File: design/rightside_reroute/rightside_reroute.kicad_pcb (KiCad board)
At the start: 4 copper layers, 144 x 96.2 mm, 197 parts, among them IC1 BQ27441DRZT-G1A, IC2 XC9148G50CER-G, IC3 nRF52833-QDAA-R7, IC4 74AHCT125PW,118, IC5 MCP23018T-E_SS, IC6 XC9291B33D1R-G, J1 USB_C_Receptacle_USB2.0_16P, J2 Battery Pos, J3 Battery Neg, J4 OLED_128x32, J6 Conn_01x04, J7 F32Q-1A7H1-11012, U2 BQ24072RGT, U3 USB6B1, U5 PEC11L-4015F-S0015, U6 PEC11L-4015F-S0015, Y1 ECS-320-8-37B2-JTY-TR

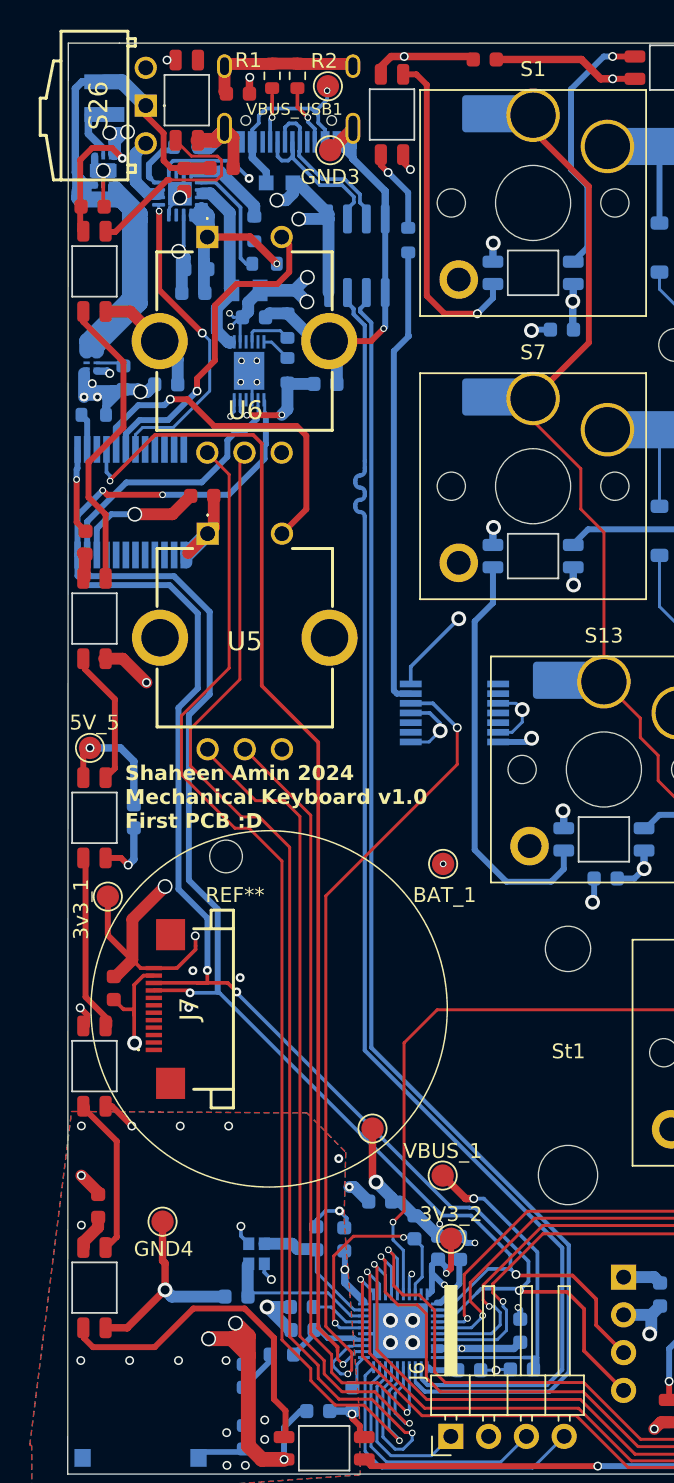
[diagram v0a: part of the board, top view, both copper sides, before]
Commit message: begin to reroute leds
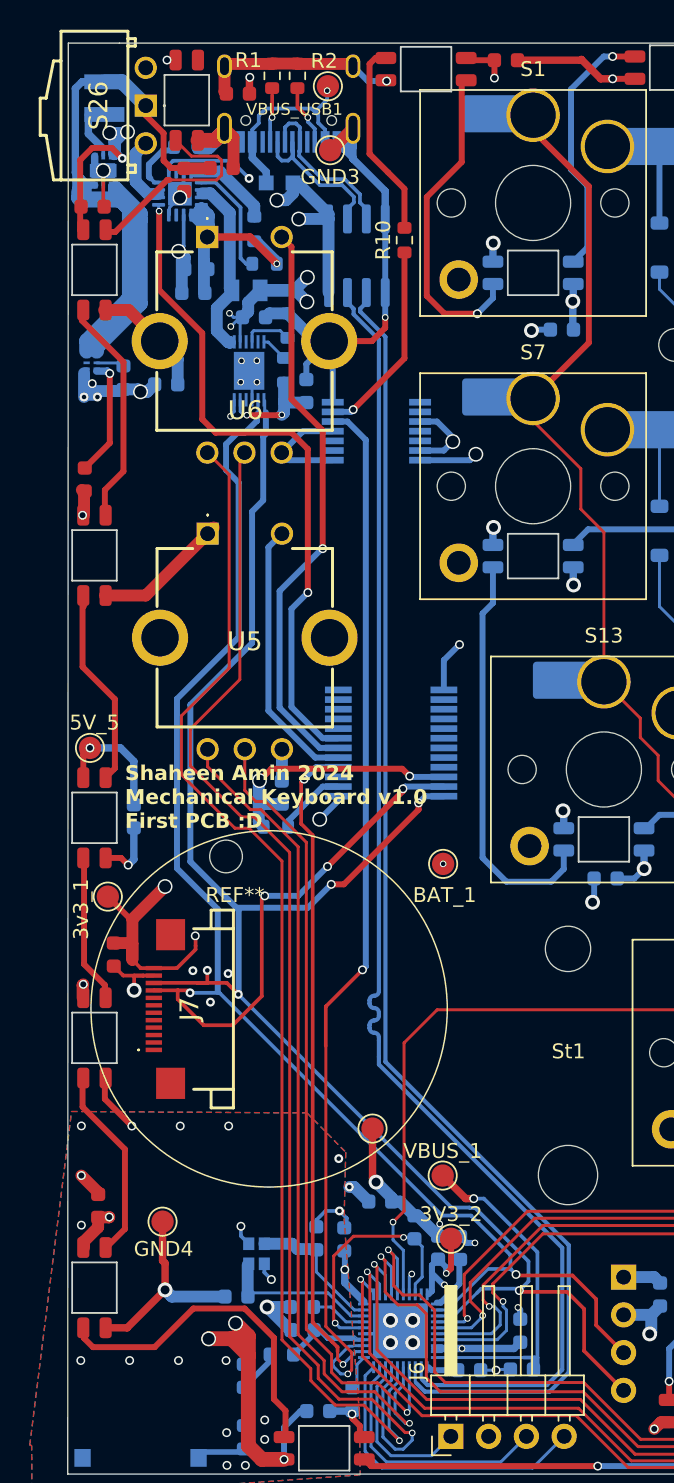
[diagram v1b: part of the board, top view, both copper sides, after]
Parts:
- C20: moved to B.Cu
- R10: moved to F.Cu
- moved R9 30.3 mm to (105.6, 89.3), turned to 180 degrees
- moved IC5 23.9 mm to (113.3, 83.7), turned to 180 degrees
- moved C20 20.7 mm to (106.0, 87.0), turned to -90 degrees
- moved IC4 19.7 mm to (112.3, 62.7)
- moved C46 4.25 mm to (92.7, 66.0)
- moved D46 4.25 mm to (93.4, 71.1)
- moved D1 3.81 mm to (115.7, 38.4), turned to 0 degrees
- moved C37 2.25 mm to (94.7, 97.9)
- moved D44 1.90 mm to (93.4, 103.5)
- moved C42 1.43 mm to (121.0, 37.8)
- moved C22 1.37 mm to (107.6, 60.0), turned to 90 degrees
- moved R10 0.25 mm to (114.2, 49.9)
- moved R8 0.23 mm to (106.1, 58.6)
- moved D47 0.10 mm to (93.4, 51.9)
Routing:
- net /INTA: track 80.1 -> 45.0 mm
- net /CHG: track 21.1 -> 45.4 mm
- net /SCL: track 104.9 -> 123.5 mm, vias 2 -> 5
- net Net-(IC4-2Y): track 31.1 -> 13.4 mm, vias 0 -> 1
- net /NO2: track 21.8 -> 39.1 mm
- net /2A: track 55.6 -> 71.4 mm
- net GND: track 291.1 -> 300.8 mm, vias 105 -> 103
- net Net-(D1-DIN): track 5.70 -> 13.3 mm, vias 1 -> 0
- net 3V3: track 76.5 -> 82.1 mm, vias 13 -> 14
- net Net-(D46-DOUT): track 20.5 -> 15.5 mm
- net Net-(D45-DOUT): track 9.10 -> 14.1 mm
- net /NO: track 22.8 -> 18.3 mm, vias 1 -> 0
- net /SDA: track 112.3 -> 115.2 mm
- net Net-(D43-DOUT): track 10.6 -> 13.1 mm
- net Net-(IC5-~{RESET}): track 2.48 -> 4.71 mm
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
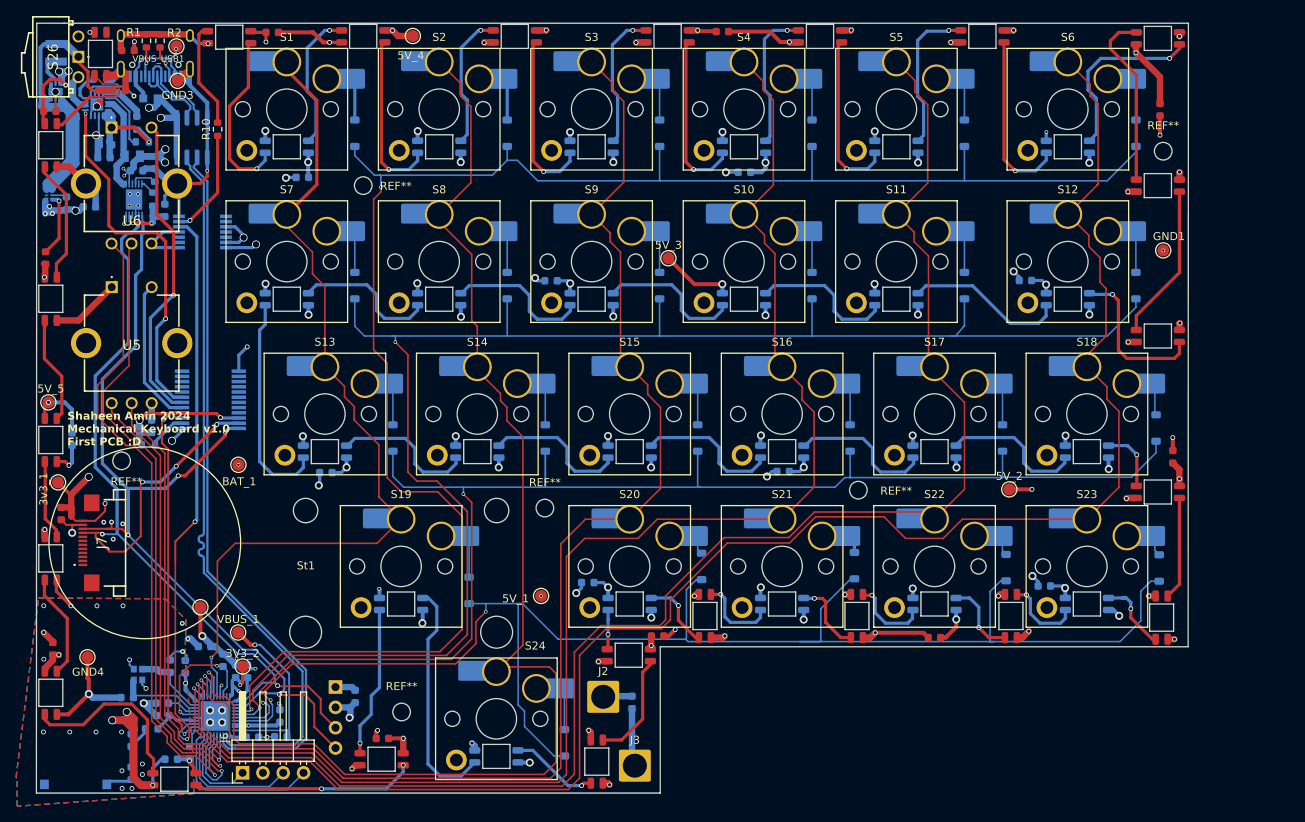
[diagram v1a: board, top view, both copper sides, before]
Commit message: prepare to add cut out for battery
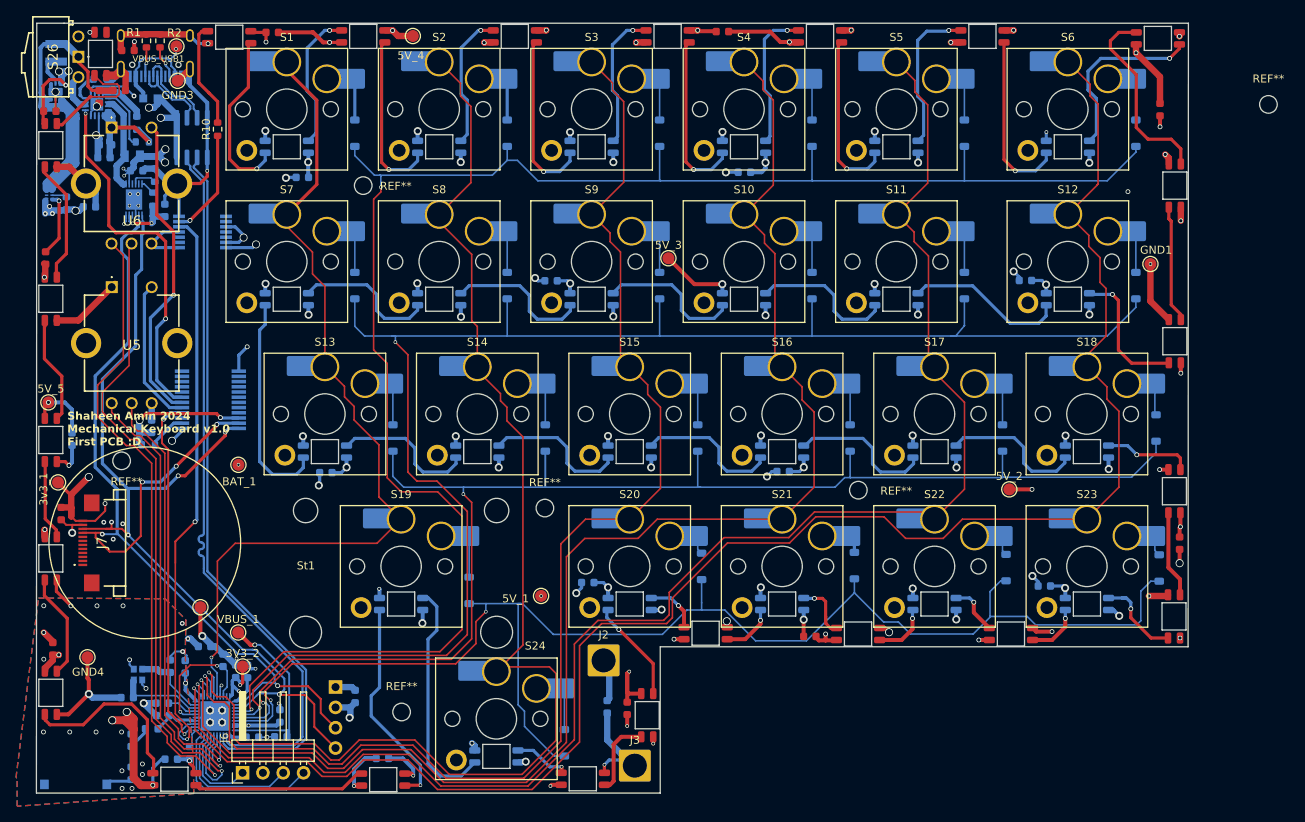
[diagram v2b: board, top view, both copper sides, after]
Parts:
- C45: moved to B.Cu
- moved C43 15.6 mm to (188.2, 113.3), turned to 180 degrees
- moved REF** 14.4 mm to (245.6, 46.8)
- moved C36 10.8 mm to (234.5, 101.6), turned to -90 degrees
- moved C44 9.82 mm to (165.4, 122.3), turned to 90 degrees
- moved D37 7.84 mm to (167.9, 123.1), turned to -90 degrees
- moved J2 4.55 mm to (162.5, 116.3)
- moved C17 3.15 mm to (162.9, 122.1)
- moved D38 2.77 mm to (159.9, 131.1), turned to 180 degrees
- moved D41 2.56 mm to (134.9, 131.2), turned to 180 degrees
- moved C45 2.50 mm to (134.8, 128.5), turned to 0 degrees
- moved GND1 2.33 mm to (230.8, 66.7)
- moved D33 2.25 mm to (194.3, 113.0), turned to 180 degrees
- moved D31 2.25 mm to (213.4, 113.0), turned to 180 degrees
- moved D15 2.22 mm to (233.9, 76.4), turned to -90 degrees
- moved D35 2.15 mm to (175.2, 112.9), turned to 180 degrees
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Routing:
- net GND: track 300.8 -> 324.8 mm, vias 103 -> 101
- net /Row 3: track 189.3 -> 177.6 mm
- net Net-(D36-DOUT): track 4.95 -> 12.9 mm
- net Net-(D40-DOUT): track 18.9 -> 26.8 mm
- net Net-(D41-DOUT): track 27.9 -> 21.7 mm, vias 2 -> 0
- net Net-(D14-DOUT): track 19.5 -> 14.7 mm
- net Net-(D38-DOUT): track 11.1 -> 7.08 mm
- net Net-(D37-DOUT): track 13.7 -> 9.78 mm
- net Net-(D34-DOUT): track 10.3 -> 6.79 mm
- net Net-(D31-DOUT): track 9.64 -> 6.46 mm
- net Net-(D27-DOUT): track 7.94 -> 11.1 mm
- net Net-(D30-DOUT): track 9.92 -> 6.88 mm
- net Net-(D32-DOUT): track 10.0 -> 7.06 mm
- net Net-(D15-DOUT): track 19.9 -> 17.2 mm
- net Net-(D35-DOUT): track 9.08 -> 6.77 mm
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
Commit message: prepare to correct bq27441
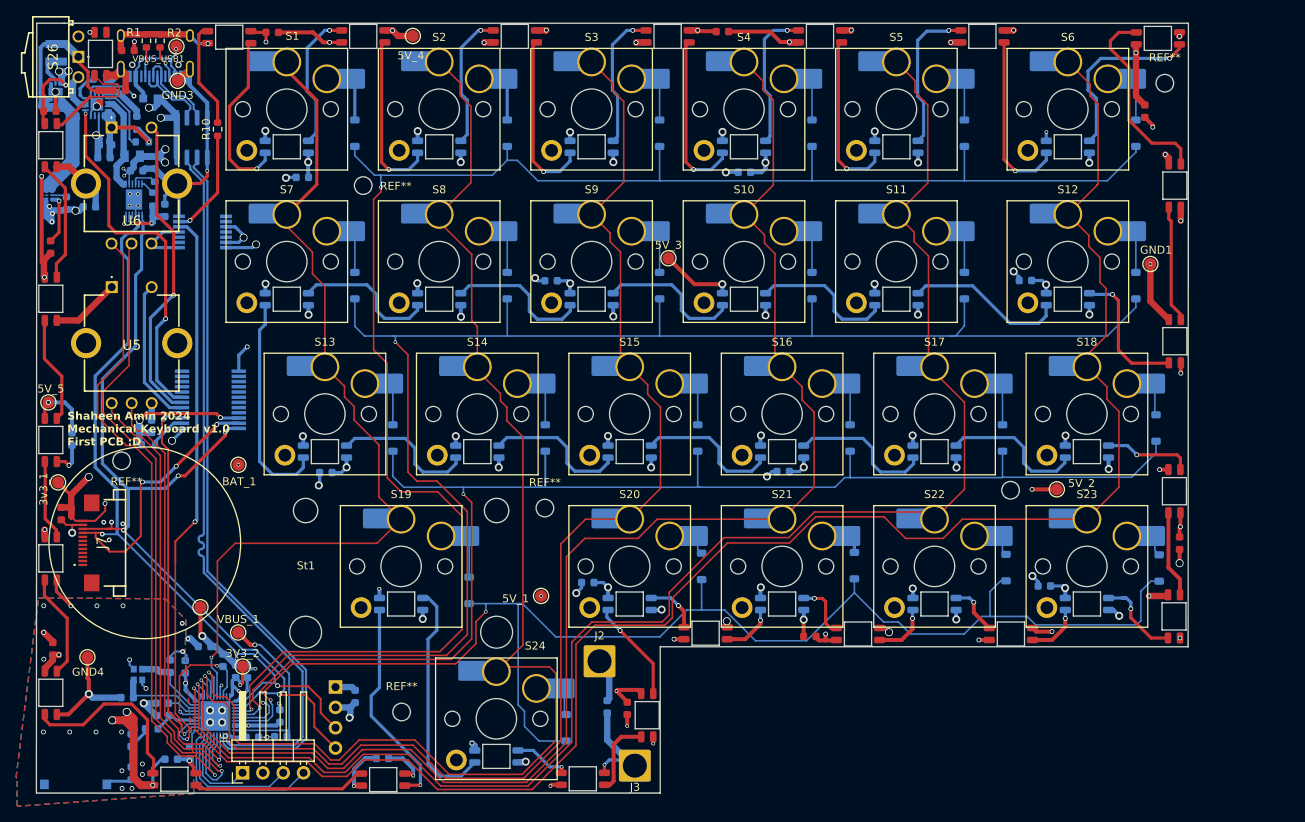
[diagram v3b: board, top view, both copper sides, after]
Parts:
- moved REF** 19.0 mm to (213.3, 95.0)
- moved REF** 13.2 mm to (232.6, 44.1)
- moved 5V_2 5.94 mm to (219.1, 94.9)
- moved C35 1.91 mm to (230.1, 47.6)
- moved Di24 1.89 mm to (157.8, 124.7)
- moved C46 1.51 mm to (93.3, 64.6)
- moved J2 0.52 mm to (161.9, 116.4)
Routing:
- net 5V: track 156.2 -> 167.0 mm, vias 57 -> 58
- net GND: track 324.8 -> 320.1 mm, vias 101 -> 100
- net 3V3: track 82.1 -> 85.9 mm
- net Net-(Di24-A): track 5.42 -> 3.62 mm

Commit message: right side backlight complete
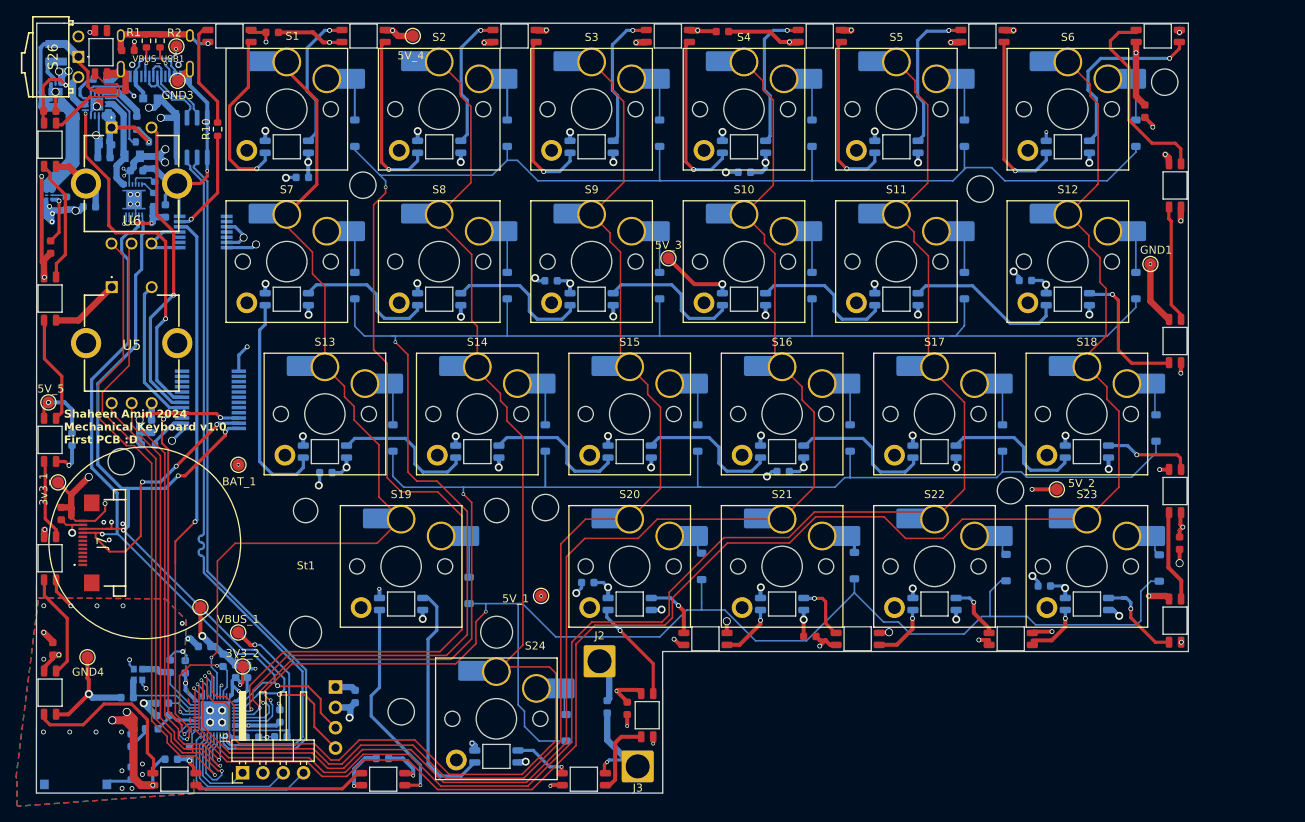
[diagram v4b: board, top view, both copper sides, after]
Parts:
- removed IC1: BQ27441DRZT-G1A, SamacSys_Parts:SON40P400X250X100-13N-D
- removed the REF** at (232.6, 44.1)
- removed the REF** at (102.2, 91.3)
- removed the REF** at (137.2, 122.7)
- removed the REF** at (155.1, 97.3)
- removed the REF** at (132.4, 56.9)
- removed the REF** at (213.3, 95.0)
- added REF**: M1.6 resin, CustomLibrary:M1.6 resin, F.Cu at (102.2, 91.5)
- added REF**: M1.6 resin, CustomLibrary:M1.6 resin, F.Cu at (155.2, 97.2)
- added REF**: M1.6 resin, CustomLibrary:M1.6 resin, F.Cu at (213.3, 95.1)
- added REF**: M1.6 resin, CustomLibrary:M1.6 resin, F.Cu at (137.2, 122.7)
- added REF**: M1.6 resin, CustomLibrary:M1.6 resin, F.Cu at (132.4, 56.9)
- added REF**: M1.6 resin, CustomLibrary:M1.6 resin, F.Cu at (209.5, 57.4)
- added REF**: M1.6 resin, CustomLibrary:M1.6 resin, F.Cu at (232.6, 44.0)
- added U1: BQ27441-G1, Package_SON:Texas_S-PDSO-N12, B.Cu at (103.8, 58.7)
- moved D35 0.71 mm to (175.2, 113.6)
- moved D33 0.61 mm to (194.2, 113.6)
- moved D31 0.61 mm to (213.3, 113.6)
- moved D29 0.55 mm to (233.9, 111.3)
- moved J3 0.37 mm to (166.7, 129.5)
- moved D13 0.30 mm to (231.7, 38.2)
- moved D48 0.23 mm to (99.6, 40.3)
- moved D1 0.15 mm to (115.7, 38.2)
- moved D38 0.14 mm to (160.0, 131.1)
- moved R8 0.12 mm to (106.2, 58.7)
- moved D47 0.11 mm to (93.3, 51.8)
- moved C22 0.10 mm to (107.7, 60.1)
- moved D46 0.09 mm to (93.3, 71.1)
- moved D44 0.09 mm to (93.3, 103.5)
- moved D43 0.09 mm to (93.3, 120.3)
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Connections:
- net /VDD renamed Net-(U1-V_{DD})
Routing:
- net GND: track 320.1 -> 318.5 mm
- net 5V: track 167.0 -> 167.9 mm
- net /SDA: track 114.9 -> 115.8 mm
- net Net-(D35-DOUT): track 6.77 -> 7.46 mm
- net Net-(D31-DOUT): track 6.46 -> 7.07 mm
- net Net-(D28-DOUT): track 10.9 -> 11.4 mm
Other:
- outline, holes or cut-outs redrawn
